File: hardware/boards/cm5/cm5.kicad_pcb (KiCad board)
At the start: 6 copper layers, 75.1 x 102 mm, 83 parts, among them J101 10164227-1001A1RLF, J102 10164227-1001A1RLF, J103 BM04B-SRSS-TB, J201 FH12-24S-0.5SVA(54), J401 1054500101, J501 USB4105-GF-A-120, J601 HR911130A, J701 1-2199230-5, M1 CM5, Q401 2N7002, SW501 SKRTLAE010, U101 SN74AHCT1G125DBVR, U301 LM61480RPHR, U401 HD3SS3220RNHR, U402 AP22652W6-7, U403 TPD4E02B04DQAR, U404 TPD4E02B04DQAR, U405 TPD4E05U06DQAR, U501 TPD4E05U06DQAR, U701 AP3441SHE-7B

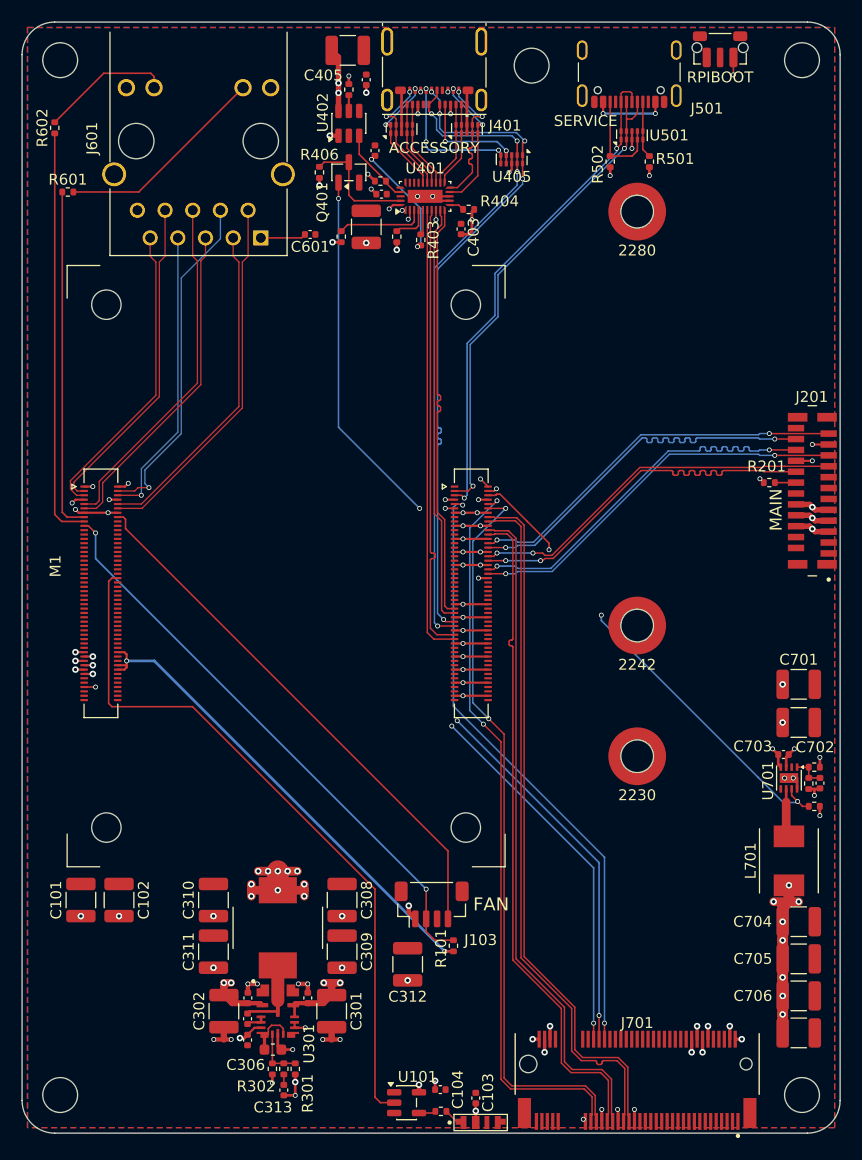
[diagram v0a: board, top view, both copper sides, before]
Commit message: fix(cm5): centre track ends and pull routes tight
Track ends meet their via and pad centres, duplicate links on the regulator and bus nets are gone,
and PCIE_CLKREQ_N (one via fewer) and PCIE_RST_N take shorter routes. The USB and Ethernet pairs
are unchanged. DRC and schematic parity pass, and every net stays joined with the zones refilled.
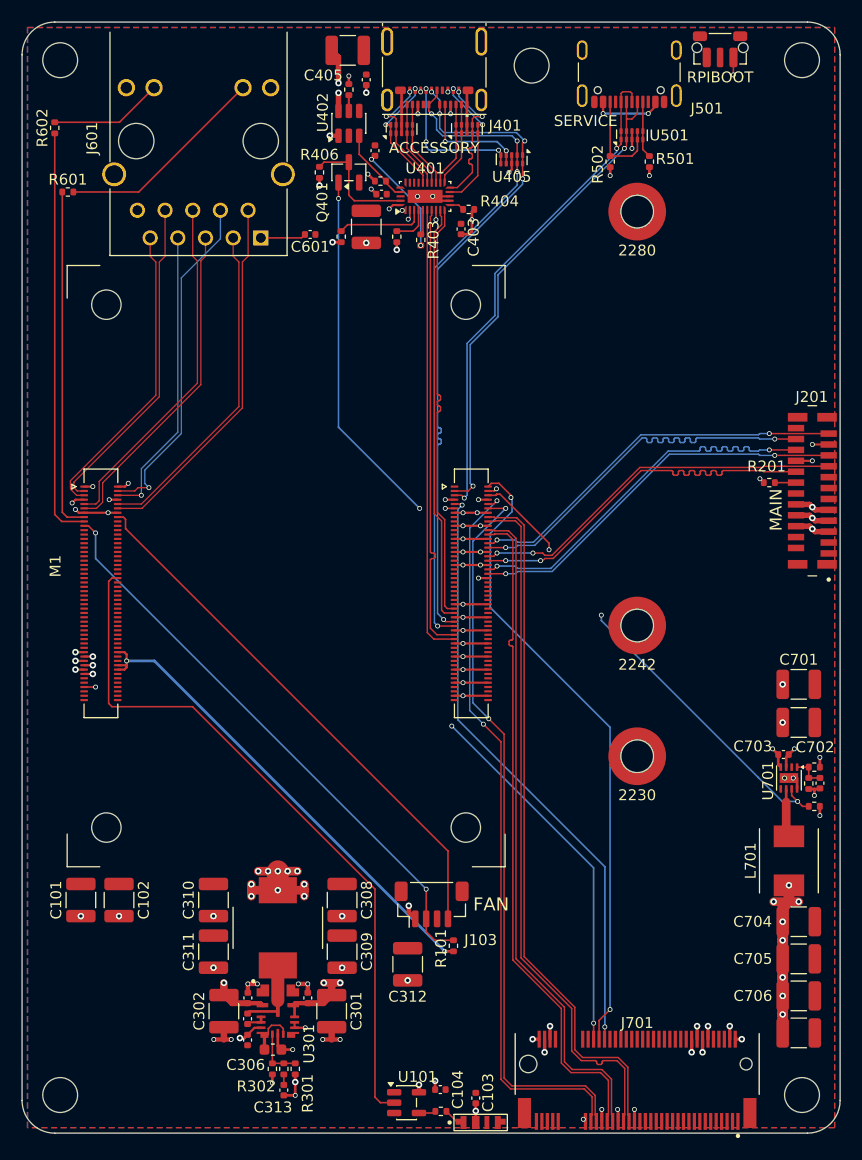
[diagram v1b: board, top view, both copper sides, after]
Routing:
- net SIDE_BUS: track 97.4 -> 94.9 mm, vias 7 -> 6
- net Net-(J601-LEDY-): track 12.1 -> 10.4 mm
- net ACC_VBUS: track 40.7 -> 39.3 mm
- net NVME_3V3: track 27.3 -> 26.1 mm
- net PCIE_CLKREQ_N: track 59.6 -> 58.5 mm, vias 3 -> 2
- net PCIE_WAKE_N: track 63.4 -> 62.4 mm
- net /5 V supply/BUCK_SW: track 7.09 -> 6.10 mm
- net PCIE_RST_N: track 56.1 -> 55.5 mm

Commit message: feat(hardware): use stocked CM5 headers
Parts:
- J201: value FH12-24S-0.5SVA(54) -> PZ200-2-10-W; footprint Iasis:Hirose_FH12-24S-0.5SVA_1x24-1MP_P0.50mm_Vertical -> Connector_PinHeader_2.00mm:PinHeader_2x10_P2.00mm_Horizontal
- moved J201 6.83 mm to (182.2, 90.3), turned to 0 degrees
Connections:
- J201 pad 10: SIDE_BUS -> GND
- J201 pad 11: GND -> SIDE_RX_N
- J201 pad 14: /Side link/CM5_HOST -> GND
- J201 pad 15: GND -> SIDE_BUS
- J201 pad 17: SIDE_D_P -> SIDE_BUS
- J201 pad 18: GND -> SIDE_D_P
- J201 pad 19: SIDE_RX_N -> SIDE_BUS
- J201 pad 20: SIDE_RX_P -> GND
- J201 pad 3: GND -> SIDE_TX_P
- J201 pad 5: SIDE_BUS -> SIDE_TX_N
- J201 pad 6: SIDE_BUS -> GND
- J201 pad 7: SIDE_BUS -> GND
- J201 pad 8: SIDE_BUS -> /Side link/CM5_HOST
- J201 pad 9: SIDE_BUS -> SIDE_RX_P
- J501 pad A4: unconnected-(J501-VBUS-PadA4) -> /Service port/VBUS_UNUSED
- J501 pad A9: unconnected-(J501-VBUS-PadA4) -> /Service port/VBUS_UNUSED
- J501 pad B4: unconnected-(J501-VBUS-PadA4) -> /Service port/VBUS_UNUSED
- J501 pad B9: unconnected-(J501-VBUS-PadA4) -> /Service port/VBUS_UNUSED
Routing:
- net SIDE_D_P: track 34.9 -> 47.9 mm, vias 2 -> 3
- net SIDE_D_N: track 34.9 -> 47.9 mm, vias 2 -> 3
- net SIDE_BUS: track 94.9 -> 84.7 mm, vias 6 -> 3
- net unconnected-(J501-VBUS-PadA4): track 6.56 -> 0.00 mm, vias 2 -> 0
- net /Service port/VBUS_UNUSED: track 0.00 -> 6.56 mm, vias 0 -> 2
- net /Side link/CM5_HOST: track 1.94 -> 6.59 mm
- net GND: track 90.9 -> 87.9 mm, vias 55 -> 53
- net SIDE_RX_P: track 35.9 -> 38.3 mm, vias 2 -> 1
- net SIDE_RX_N: track 35.9 -> 38.3 mm, vias 2 -> 1
- net SIDE_TX_N: track 35.6 -> 33.8 mm, vias 2 -> 1
- net SIDE_TX_P: track 35.6 -> 33.8 mm, vias 2 -> 1
- net VBUS_EN: track 71.9 -> 72.4 mm

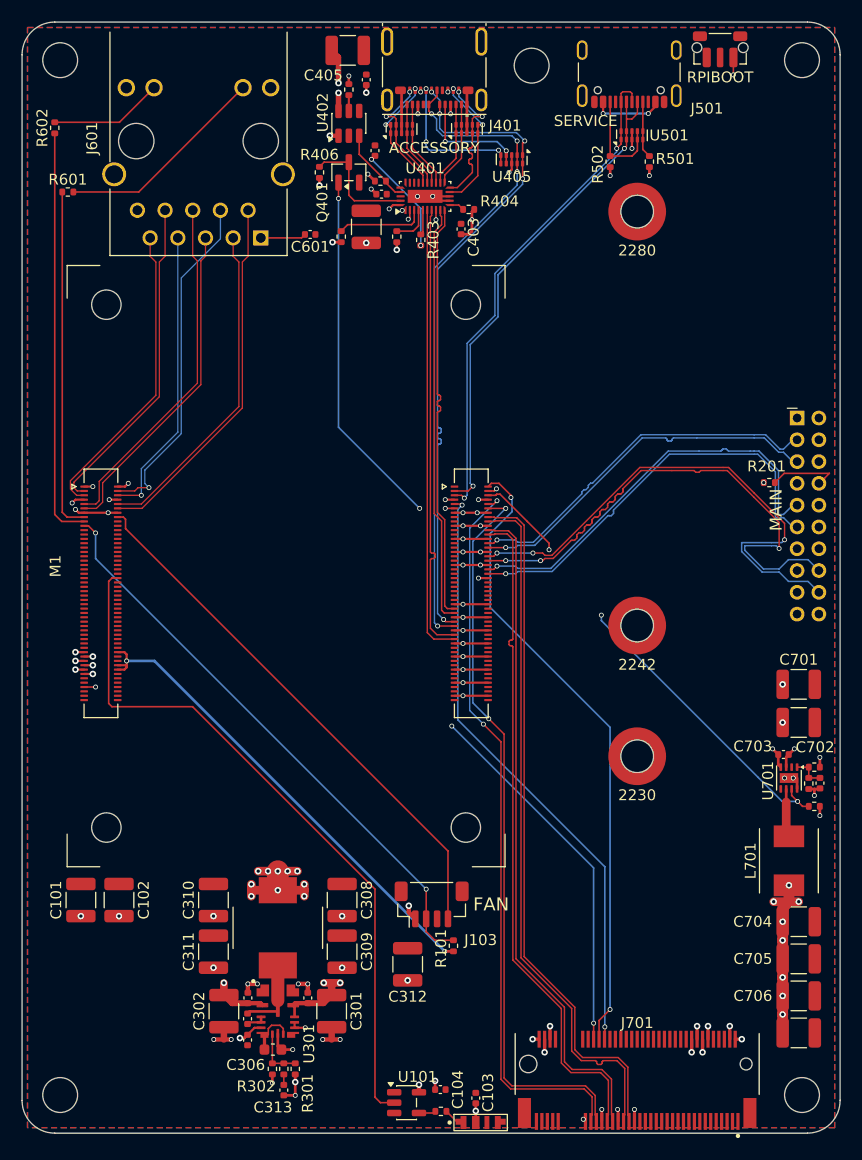
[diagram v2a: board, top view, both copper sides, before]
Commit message: fix(hardware): clean up routing on both boards
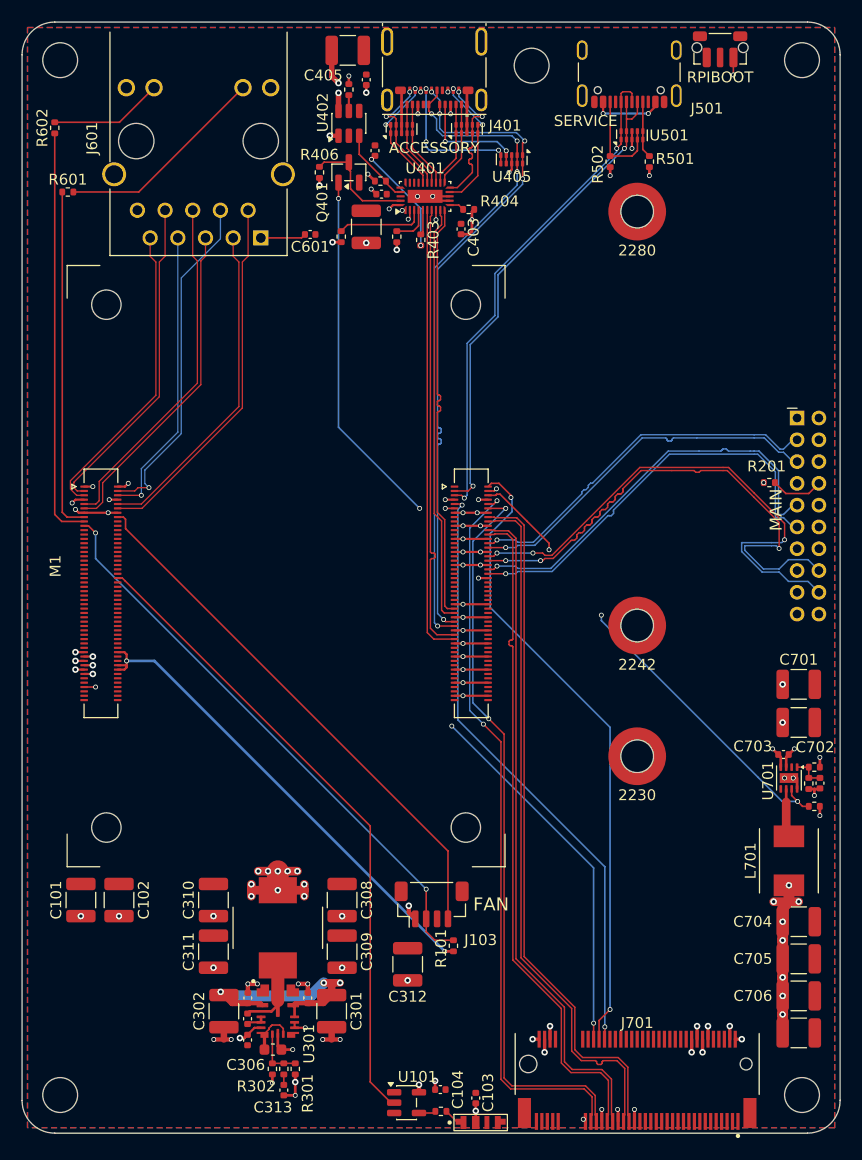
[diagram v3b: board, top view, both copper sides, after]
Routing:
- net /Compute module/LED_DATA: track 64.7 -> 59.1 mm
- net SIDE_BUS: track 84.7 -> 82.5 mm
- net /Side link/CM5_HOST: track 6.59 -> 4.84 mm
- net VBUS_EN: track 72.4 -> 71.4 mm
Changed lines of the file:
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@@
 	)
 	(segment
+		(start 180.65 121.47)
+		(end 180.65 122.4)
+		(width 0.25)
+		(layer "F.Cu")
+		(net "GND")
+	)
+	(segment
 		(start 151.48 100.245)
 		(end 153.08 100.245)
@@
 	)
 	(segment
+		(start 180.42 121.24)
+		(end 180.65 121.47)
+		(width 0.25)
+		(layer "F.Cu")
+		(net "GND")
+	)
+	(segment
 		(start 139.42 146.275)
 		(end 139.42 147.4)
@@
 	)
 	(segment
-		(start 180.42 122.17)
-		(end 180.42 121.24)
-		(width 0.25)
-		(layer "F.Cu")
-		(net "GND")
-	)
-	(segment
 		(start 151.48 113.445)
 		(end 153.78 113.445)
@@
 	)
 	(segment
-		(start 180.65 122.4)
-		(end 180.42 122.17)
-		(width 0.25)
-		(layer "F.Cu")
-		(net "GND")
-	)
-	(segment
 		(start 162.72 154.925)
 		(end 162.52 154.725)
@@
 	)
 	(segment
-		(start 147.5 95)
-		(end 148 94.5)
-		(width 0.15)
-		(layer "In3.Cu")
-		(net "VBUS_EN")
-	)
-	(segment
 		(start 147.5 98.645)
-		(end 147.5 95)
-		(width 0.15)
-		(layer "In3.Cu")
-		(net "VBUS_EN")
-	)
-	(segment
-		(start 148 94.5)
-		(end 177.31 94.5)
+		(end 147.5 95.39)
 		(width 0.15)
 		(layer "In3.Cu")
@@
 	)
 	(segment
-		(start 177.31 94.5)
+		(start 147.5 95.39)
 		(end 178.2 95.39)
 		(width 0.15)
@@
 	)
 	(segment
-		(start 141 69.9)
-		(end 141 66.8625)
+		(start 141.15 67.7)
+		(end 141 67.55)
 		(width 0.15)
 		(layer "F.Cu")
@@
 	)
 	(segment
-		(start 141.5 70.4)
-		(end 141 69.9)
+		(start 141.15 69.3)
+		(end 141.15 67.7)
 		(width 0.15)
 		(layer "F.Cu")
@@
 	(segment
 		(start 145.75 70.4)
-		(end 141.5 70.4)
+		(end 142.25 70.4)
+		(width 0.15)
+		(layer "F.Cu")
+		(net "/Accessory port/CC_EN_N")
+	)
+	(segment
+		(start 141 67.55)
+		(end 141 66.8625)
 		(width 0.15)
 		(layer "F.Cu")
@@
 	)
 	(segment
+		(start 142.25 70.4)
+		(end 141.15 69.3)
+		(width 0.15)
+		(layer "F.Cu")
+		(net "/Accessory port/CC_EN_N")
+	)
+	(segment
 		(start 141 66.8625)
 		(end 138.7275 66.8625)
@@
 	)
 	(segment
-		(start 140.05 59.6)
-		(end 140.05 57.22)
+		(start 139.425 58.975)
+		(end 140.05 59.6)
 		(width 0.5)
 		(layer "F.Cu")
@@
 	)
 	(segment
-		(start 150.34 61.565)
-		(end 150.34 62.425)
-		(width 0.25)
+		(start 139.425 58.975)
+		(end 139.425 56.6)
+		(width 0.5)
 		(layer "F.Cu")
 		(net "ACC_VBUS")
 	)
 	(segment
-		(start 140.05 57.22)
-		(end 139.425 56.6)
-		(width 0.5)
+		(start 150.34 61.565)
+		(end 150.34 62.425)
+		(width 0.25)
 		(layer "F.Cu")
 		(net "ACC_VBUS")
@@
 	)
 	(segment
-		(start 129.53 142.2)
-		(end 129.53 143.325)
-		(width 0.7)
-		(layer "F.Cu")
-		(net "SIDE_BUS")
-	)
-	(segment
 		(start 132.8875 144.07)
 		(end 133.0675 144.25)
@@
 	)
 	(via
-		(at 138.7 142.2)
+		(at 129.23 143.03)
 		(size 0.6)
 		(drill 0.3)
@@
 	)
 	(via
-		(at 129.53 142.2)
+		(at 138.7 142.2)
 		(size 0.6)
 		(drill 0.3)
@@
 	)
 	(segment
+		(start 137.5 143.4)
+		(end 129.9 143.4)
+		(width 1)
+		(layer "B.Cu")
+		(net "SIDE_BUS")
+	)
+	(segment
+		(start 138.7 142.2)
+		(end 137.5 143.4)
+		(width 1)
+		(layer "B.Cu")
+		(net "SIDE_BUS")
+	)
+	(segment
 		(start 178.2 105.2)
 		(end 181.3 105.2)
@@
 	)
 	(segment
-		(start 138.7 142.2)
-		(end 137.3 143.6)
-		(width 1)
-		(layer "In3.Cu")
-		(net "SIDE_BUS")
-	)
-	(segment
-		(start 130.2 142.2)
-		(end 129.53 142.2)
-		(width 1)
-		(layer "In3.Cu")
-		(net "SIDE_BUS")
-	)
-	(segment
 		(start 182.15 104.35)
 		(end 182.15 108.35)
@@
 	)
 	(segment
-		(start 131.6 143.6)
-		(end 130.2 142.2)
-		(width 1)
-		(layer "In3.Cu")
-		(net "SIDE_BUS")
-	)
-	(segment
-		(start 137.3 143.6)
-		(end 131.6 143.6)
-		(width 1)
-		(layer "In3.Cu")
-		(net "SIDE_BUS")
-	)
-	(segment
 		(start 131.855 145.825)
 		(end 131.7 145.98)
@@
 	)
 	(segment
+		(start 133.855 146.175)
+		(end 133.955 146.075)
+		(width 0.15)
+		(layer "F.Cu")
+		(net "Net-(U301-RT)")
+	)
+	(segment
 		(start 133.255 146.975)
-		(end 133.255 148.33)
-		(width 0.3)
+		(end 133.255 146.875)
+		(width 0.15)
 		(layer "F.Cu")
 		(net "Net-(U301-RT)")
 	)
 	(segment
-		(start 134.68 146.1)
-		(end 133.905 146.1)
+		(start 133.955 146.075)
+		(end 134.655 146.075)
 		(width 0.15)
 		(layer "F.Cu")
@@
 	)
 	(segment
-		(start 133.605 146.4)
-		(end 133.605 146.975)
+		(start 134.98 146.4)
+		(end 134.98 146.9125)
 		(width 0.15)
 		(layer "F.Cu")
@@
 	)
 	(segment
-		(start 133.905 146.1)
-		(end 133.605 146.4)
+		(start 134.655 146.075)
+		(end 134.98 146.4)
 		(width 0.15)
 		(layer "F.Cu")
@@
 	)
 	(segment
-		(start 134.98 146.4)
-		(end 134.68 146.1)
+		(start 133.255 146.875)
+		(end 133.655 146.475)
 		(width 0.15)
 		(layer "F.Cu")
@@
 	)
 	(segment
-		(start 134.98 146.9125)
-		(end 134.98 146.4)
+		(start 133.655 146.475)
+		(end 133.655 146.375)
+		(width 0.15)
+		(layer "F.Cu")
+		(net "Net-(U301-RT)")
+	)
+	(segment
+		(start 133.255 146.975)
+		(end 133.255 148.33)
+		(width 0.3)
+		(layer "F.Cu")
+		(net "Net-(U301-RT)")
+	)
+	(segment
+		(start 133.655 146.375)
+		(end 133.855 146.175)
 		(width 0.15)
 		(layer "F.Cu")
@@
 	)
 	(segment
+		(start 133.9 144.82)
+		(end 134.48 144.24)
+		(width 0.25)
+		(layer "F.Cu")
+		(net "/5 V supply/BUCK_SW")
+	)
+	(segment
 		(start 131.7 145.02)
-		(end 131.895 144.825)
+		(end 131.9 144.82)
 		(width 0.25)
 		(layer "F.Cu")
@@
 	)
 	(segment
-		(start 131.895 144.825)
-		(end 134.48 144.825)
+		(start 131.9 144.82)
+		(end 133.9 144.82)
 		(width 0.25)
 		(layer "F.Cu")
@@
 	)
 	(segment
-		(start 185.11 95.43)
-		(end 184.66 95.88)
+		(start 183.22 97.28)
+		(end 184.15 96.35)
 		(width 0.15)
 		(layer "F.Cu")
@@
 	)
 	(segment
-		(start 184.66 95.88)
-		(end 184.66 96.48)
-		(width 0.15)
-		(layer "F.Cu")
-		(net "/Side link/CM5_HOST")
-	)
-	(segment
-		(start 180.96 95.43)
-		(end 185.11 95.43)
+		(start 181.11 97.28)
+		(end 183.22 97.28)
 		(width 0.15)
 		(layer "F.Cu")
@@
 	(segment
 		(start 180.11 96.28)
-		(end 180.96 95.43)
+		(end 181.11 97.28)
 		(width 0.15)
 		(layer "F.Cu")
@@
 	)
 	(segment
-		(start 119.78 105.045)
-		(end 119.25 105.045)
-		(width 0.15)
-		(layer "F.Cu")
-		(net "/Compute module/LED_DATA")
-	)
-	(segment
-		(start 143.4 133.6)
-		(end 143.4 152.7)
-		(width 0.15)
-		(layer "F.Cu")
-		(net "/Compute module/LED_DATA")
-	)
-	(segment
-		(start 126.65 116.85)
-		(end 143.4 133.6)
+		(start 142.9625 127.8)
+		(end 120.4625 105.3)
 		(width 0.15)
 		(layer "F.Cu")
@@
 	)
 	(segment
-		(start 119.25 105.045)
-		(end 118.95 105.345)
+		(start 142.9625 151.3)
+		(end 142.9625 127.8)
 		(width 0.15)
 		(layer "F.Cu")
@@
 	)
 	(segment
-		(start 118.95 116.55)
-		(end 119.25 116.85)
+		(start 120.4625 105.3)
+		(end 120.2075 105.045)
 		(width 0.15)
 		(layer "F.Cu")
@@
 	)
 	(segment
-		(start 143.9 153.2)
-		(end 145.1625 153.2)
+		(start 144.8625 153.2)
+		(end 142.9625 151.3)
 		(width 0.15)
 		(layer "F.Cu")
@@
 	)
 	(segment
-		(start 143.4 152.7)
-		(end 143.9 153.2)
+		(start 120.2075 105.045)
+		(end 119.78 105.045)
 		(width 0.15)
 		(layer "F.Cu")
@@
 	)
 	(segment
-		(start 119.25 116.85)
-		(end 126.65 116.85)
-		(width 0.15)
-		(layer "F.Cu")
-		(net "/Compute module/LED_DATA")
-	)
-	(segment
-		(start 118.95 105.345)
-		(end 118.95 116.55)
+		(start 145.1625 153.2)
+		(end 144.8625 153.2)
 		(width 0.15)
 		(layer "F.Cu")
@@
 	)
 	(via
-		(at 164.34 62.4)
+		(at 168.49 62.4)
 		(size 0.45)
 		(drill 0.3)
@@
 	)
 	(via
-		(at 168.49 62.4)
+		(at 164.34 62.4)
 		(size 0.45)
 		(drill 0.3)
